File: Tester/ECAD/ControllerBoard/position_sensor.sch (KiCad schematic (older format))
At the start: 0 parts

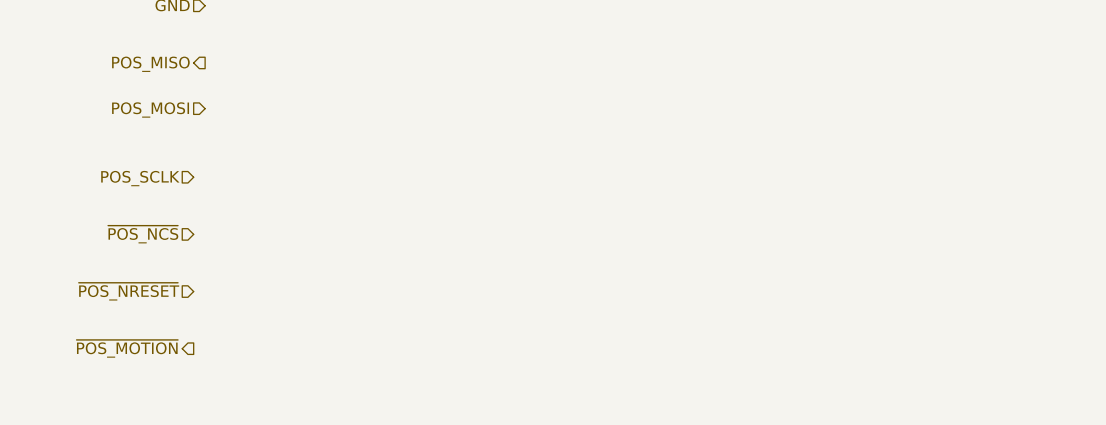
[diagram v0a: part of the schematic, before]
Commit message: Progressed circuit layout.
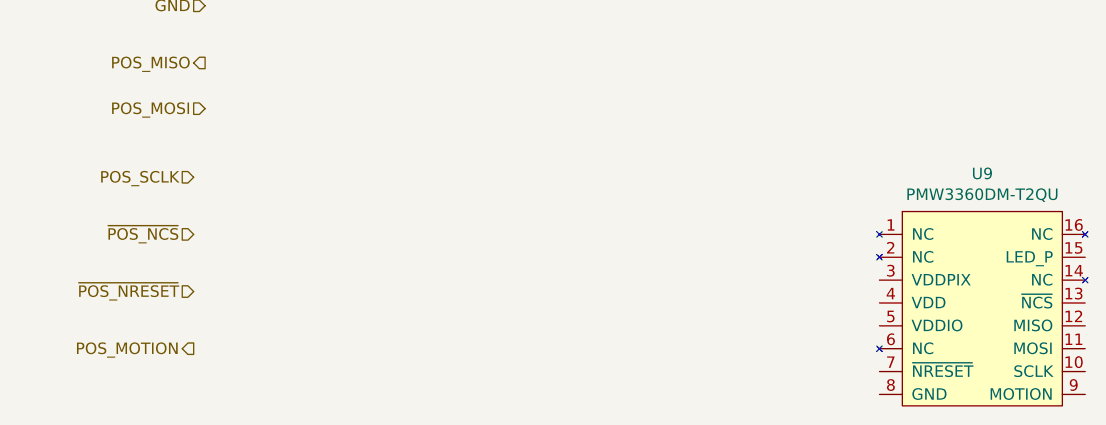
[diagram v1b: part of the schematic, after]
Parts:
- added U9: PMW3360DM-T2QU, PixArt:PMW3360DM-T2QU, symbol PixArt:PMW3360DM-T2QU
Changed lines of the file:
@@
 ~POS_NRESET
 Text HLabel 3200 3350 0    50   Output ~ 0
-~POS_MOTION
+POS_MOTION
+$Comp
+L PixArt:PMW3360DM-T2QU U9
+U 1 1 5E9F77F4
+P 6650 3300
+F 0 "U9" H 6650 4015 50  0000 C CNN
+F 1 "PMW3360DM-T2QU" H 6650 3924 50  0000 C CNN
+F 2 "PixArt:PMW3360DM-T2QU" H 6650 3300 50  0001 C CNN
+F 3 "" H 6650 3300 50  0001 C CNN
+	1    6650 3300
+	1    0    0    -1
+$EndComp
 $EndSCHEMATC

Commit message: Progressed circuit updates.
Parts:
- added C2, C4: 1uC, Capacitor_SMD:C_0805_2012Metric_Pad1.15x1.40mm_HandSolder, symbol Device:C
- added C22, C28: 0.1uC, Capacitor_SMD:C_0805_2012Metric_Pad1.15x1.40mm_HandSolder, symbol Device:C
- added C23, C6: 4.7uC, Capacitor_SMD:C_0805_2012Metric_Pad1.15x1.40mm_HandSolder, symbol Device:C
- added R2, R4: 39R, Resistor_SMD:R_0805_2012Metric_Pad1.15x1.40mm_HandSolder, symbol Device:R
- added U11: TLV70019_SOT23-5, Package_TO_SOT_SMD:SOT-23-5, symbol Regulator_Linear:TLV70019_SOT23-5
- added U4: PMW3360DM-T2QU, PixArt:PMW3360DM-T2QU, symbol PixArt:PMW3360DM-T2QU
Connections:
- net GND: now also U9.8 (GND), C2.2, C22.2, C23.2, C28.2, C4.2, C6.2, U11.2 (GND), U4.8 (GND)
- net at U9.15 (LED_P): now also R2.2
- net at U9.3 (VDDPIX): now also C22.1, C6.1
- net V1_9: now reaches U9.4 (VDD)
- net V1_9: now also U9.5 (VDDIO), C2.1, R2.1, R4.1, U11.5 (OUT), U4.4 (VDD), U4.5 (VDDIO)
- new net: R4.2, U4.15 (LED_P)
- new net: C23.1, C28.1, U4.3 (VDDPIX)
- new net V5_0: C4.1, U11.1 (IN), U11.3 (EN)
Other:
- moved on the sheet: U9

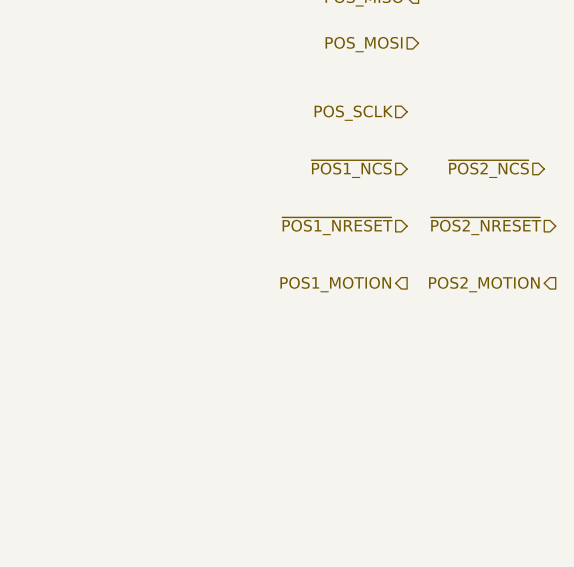
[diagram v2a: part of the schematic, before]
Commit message: Progressed circuit layout.
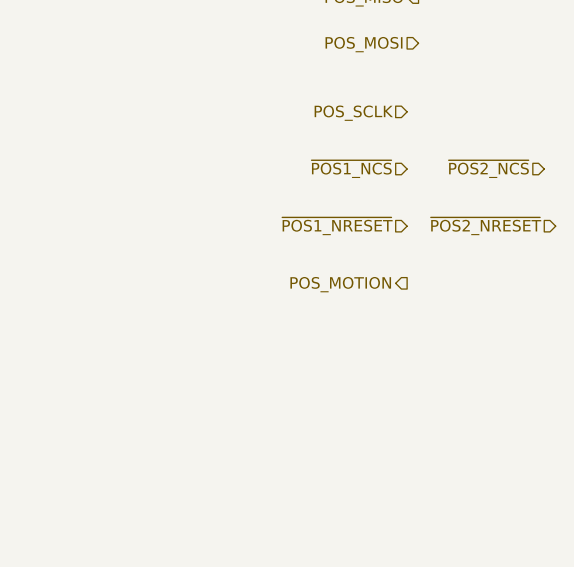
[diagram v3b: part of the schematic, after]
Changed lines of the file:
@@
 ~POS1_NRESET
 Text HLabel 9300 4150 0    50   Output ~ 0
-POS1_MOTION
+POS_MOTION
 $Comp
 L PixArt:PMW3360DM-T2QU U9
@@
 Text HLabel 9950 3900 0    50   Input ~ 0
 ~POS2_NRESET
-Text HLabel 9950 4150 0    50   Output ~ 0
-POS2_MOTION
 $Comp
 L Device:C C2

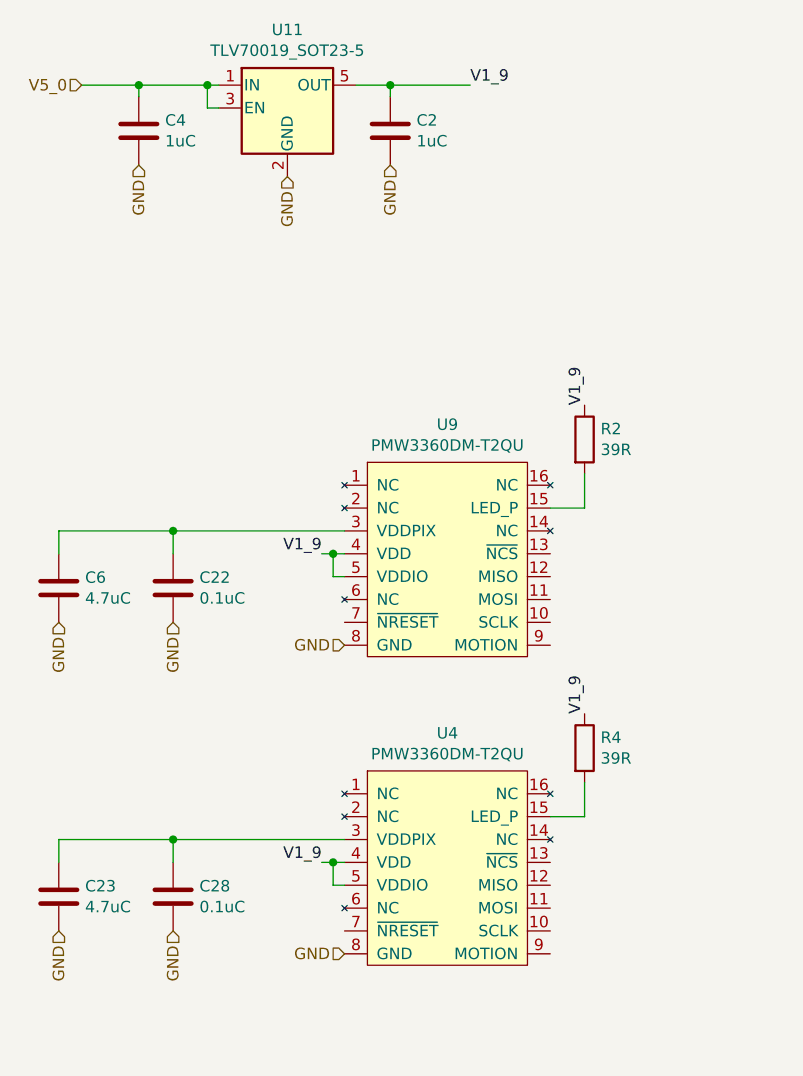
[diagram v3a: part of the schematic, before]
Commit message: Progressed circuit layout.
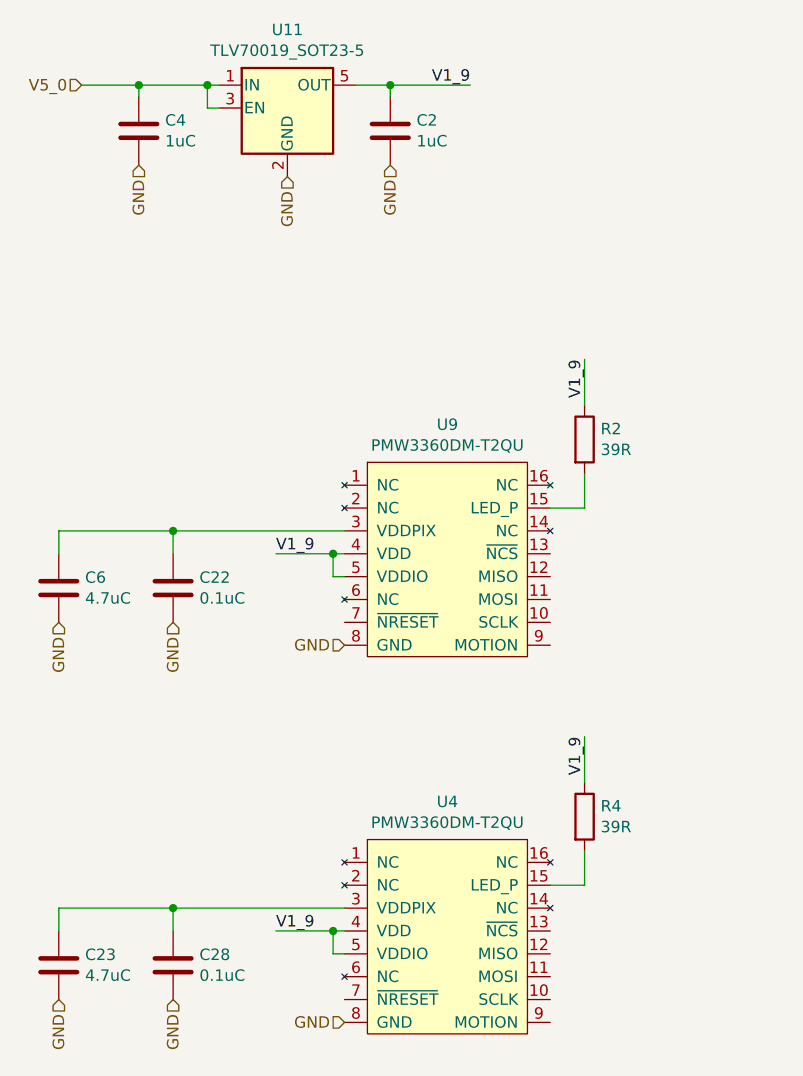
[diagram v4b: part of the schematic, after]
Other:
- moved on the sheet: C23, C28, R4, U4
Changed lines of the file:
@@
 L PixArt:PMW3360DM-T2QU U4
 U 1 1 5EA18837
-P 4100 5450
-F 0 "U4" H 4100 6165 50  0000 C CNN
-F 1 "PMW3360DM-T2QU" H 4100 6074 50  0000 C CNN
-F 2 "PixArt:PMW3360DM-T2QU" H 4100 5450 50  0001 C CNN
-F 3 "" H 4100 5450 50  0001 C CNN
-	1    4100 5450
+P 4100 5750
+F 0 "U4" H 4100 6465 50  0000 C CNN
+F 1 "PMW3360DM-T2QU" H 4100 6374 50  0000 C CNN
+F 2 "PixArt:PMW3360DM-T2QU" H 4100 5750 50  0001 C CNN
+F 3 "" H 4100 5750 50  0001 C CNN
+	1    4100 5750
 	1    0    0    -1
 $EndComp
@@
 L Device:R R4
 U 1 1 5EA148DB
-P 4700 4800
-F 0 "R4" H 4770 4846 50  0000 L CNN
-F 1 "39R" H 4770 4755 50  0000 L CNN
-F 2 "Resistor_SMD:R_0805_2012Metric_Pad1.15x1.40mm_HandSolder" V 4630 4800 50  0001 C CNN
-F 3 "~" H 4700 4800 50  0001 C CNN
-F 4 "RC0805FR-0739RL" H 4700 4800 50  0001 C CNN "Manufacturer Part Number"
-	1    4700 4800
+P 4700 5100
+F 0 "R4" H 4770 5146 50  0000 L CNN
+F 1 "39R" H 4770 5055 50  0000 L CNN
+F 2 "Resistor_SMD:R_0805_2012Metric_Pad1.15x1.40mm_HandSolder" V 4630 5100 50  0001 C CNN
+F 3 "~" H 4700 5100 50  0001 C CNN
+F 4 "RC0805FR-0739RL" H 4700 5100 50  0001 C CNN "Manufacturer Part Number"
+	1    4700 5100
 	1    0    0    -1
 $EndComp
@@
 L Device:C C23
 U 1 1 5EA148E2
-P 2400 5450
-F 0 "C23" H 2515 5496 50  0000 L CNN
-F 1 "4.7uC" H 2515 5405 50  0000 L CNN
-F 2 "Capacitor_SMD:C_0805_2012Metric_Pad1.15x1.40mm_HandSolder" H 2438 5300 50  0001 C CNN
-F 3 "~" H 2400 5450 50  0001 C CNN
-F 4 "C0805C475K9PACTU" H 2400 5450 50  0001 C CNN "Manufacturer Part Number"
-	1    2400 5450
+P 2400 5750
+F 0 "C23" H 2515 5796 50  0000 L CNN
+F 1 "4.7uC" H 2515 5705 50  0000 L CNN
+F 2 "Capacitor_SMD:C_0805_2012Metric_Pad1.15x1.40mm_HandSolder" H 2438 5600 50  0001 C CNN
+F 3 "~" H 2400 5750 50  0001 C CNN
+F 4 "C0805C475K9PACTU" H 2400 5750 50  0001 C CNN "Manufacturer Part Number"
+	1    2400 5750
 	1    0    0    -1
 $EndComp
@@
 L Device:C C28
 U 1 1 5EA148E9
-P 2900 5450
-F 0 "C28" H 3015 5496 50  0000 L CNN
-F 1 "0.1uC" H 3015 5405 50  0000 L CNN
-F 2 "Capacitor_SMD:C_0805_2012Metric_Pad1.15x1.40mm_HandSolder" H 2938 5300 50  0001 C CNN
-F 3 "~" H 2900 5450 50  0001 C CNN
-F 4 "CC0805ZRY5V8BB104" H 2900 5450 50  0001 C CNN "Manufacturer Part Number"
-	1    2900 5450
+P 2900 5750
+F 0 "C28" H 3015 5796 50  0000 L CNN
+F 1 "0.1uC" H 3015 5705 50  0000 L CNN
+F 2 "Capacitor_SMD:C_0805_2012Metric_Pad1.15x1.40mm_HandSolder" H 2938 5600 50  0001 C CNN
+F 3 "~" H 2900 5750 50  0001 C CNN
+F 4 "CC0805ZRY5V8BB104" H 2900 5750 50  0001 C CNN "Manufacturer Part Number"
+	1    2900 5750
 	1    0    0    -1
 $EndComp
@@
 	3850 1900 4200 1900
 Connection ~ 3850 1900
-Text Label 4200 1900 0    50   ~ 0
+Text Label 4200 1900 2    50   ~ 0
 V1_9
 Wire Wire Line
@@
 Wire Wire Line
 	3600 3950 3650 3950
-Wire Wire Line
-	3600 3950 3550 3950
 Connection ~ 3600 3950
-Text Label 3550 3950 2    50   ~ 0
+Text Label 3350 3950 0    50   ~ 0
 V1_9
 Wire Wire Line
@@
 Wire Wire Line
 	4700 3750 4700 3600
-Text Label 4700 3300 1    50   ~ 0
-V1_9
-Wire Wire Line
-	2400 5300 2400 5200
-Wire Wire Line
-	2400 5200 2900 5200
-Wire Wire Line
-	2900 5300 2900 5200
-Connection ~ 2900 5200
-Wire Wire Line
-	2900 5200 3650 5200
-Wire Wire Line
-	3650 5400 3600 5400
-Wire Wire Line
-	3600 5400 3600 5300
-Wire Wire Line
-	3600 5300 3650 5300
-Wire Wire Line
-	3600 5300 3550 5300
-Connection ~ 3600 5300
-Text HLabel 2400 5600 3    50   Input ~ 0
-GND
-Text HLabel 2900 5600 3    50   Input ~ 0
-GND
-Wire Wire Line
-	4700 4950 4700 5100
-Wire Wire Line
-	4700 5100 4550 5100
-Text Label 3550 5300 2    50   ~ 0
-V1_9
-Text Label 4700 4650 1    50   ~ 0
-V1_9
-Text HLabel 3650 5700 0    50   Input ~ 0
-GND
+Text Label 4700 3100 3    50   ~ 0
+V1_9
+Wire Wire Line
+	2400 5600 2400 5500
+Wire Wire Line
+	2400 5500 2900 5500
+Wire Wire Line
+	2900 5600 2900 5500
+Connection ~ 2900 5500
+Wire Wire Line
+	2900 5500 3650 5500
+Wire Wire Line
+	3650 5700 3600 5700
+Wire Wire Line
+	3600 5700 3600 5600
+Wire Wire Line
+	3600 5600 3650 5600
+Connection ~ 3600 5600
+Text HLabel 2400 5900 3    50   Input ~ 0
+GND
+Text HLabel 2900 5900 3    50   Input ~ 0
+GND
+Wire Wire Line
+	4700 5250 4700 5400
+Wire Wire Line
+	4700 5400 4550 5400
+Text Label 3350 5600 0    50   ~ 0
+V1_9
+Text Label 4700 4750 3    50   ~ 0
+V1_9
+Text HLabel 3650 6000 0    50   Input ~ 0
+GND
+Wire Wire Line
+	4700 3300 4700 3100
+Wire Wire Line
+	4700 4950 4700 4750
+Wire Wire Line
+	3350 3950 3600 3950
+Wire Wire Line
+	3350 5600 3600 5600
 $EndSCHEMATC

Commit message: Progressed circuit layout.
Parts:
- added C31, C32, C33, C34: 0.1uC, Capacitor_SMD:C_0805_2012Metric_Pad1.15x1.40mm_HandSolder, symbol Device:C
- added U12, U8: SN74AVC4T245PW, Package_SO:SOIC-16_3.9x9.9mm_P1.27mm, symbol Logic_LevelTranslator:SN74AVC4T245PW
- added U13: 74LVC1G32, Package_TO_SOT_SMD:SOT-353_SC-70-5_Handsoldering, symbol 74xGxx:74LVC1G32
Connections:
- net labels added: V3_3
- wire segments 31 -> 87
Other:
- moved on the sheet: C2, C22, C23, C28, C4, C6, R2, R4, U11, U4, U9
